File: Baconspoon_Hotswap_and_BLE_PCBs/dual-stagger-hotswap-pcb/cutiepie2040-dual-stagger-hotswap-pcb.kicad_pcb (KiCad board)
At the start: 2 copper layers, 200 x 81 mm, 119 parts, among them J1 SM04B-SRSS-TB(LF)(SN), J2 SWD, SW1 BOOT, SW2 RESET, U1 RP2040, U2 W25Q128JVS, U3 XC6206P332MR, Y1 12MHz

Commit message: upload accurate fabrication files for dual-stagger hotswap PCB
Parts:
- MX49: moved to B.Cu
- SW1: value BOOT -> BOOTSEL
- turned MX49 to 180 degrees
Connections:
- MX41 pad 2: unconnected-(MX41-ROW-Pad2) -> Net-(D7-A)
- MX42 pad 2: unconnected-(MX42-ROW-Pad2) -> Net-(D11-A)
- MX43 pad 2: unconnected-(MX43-ROW-Pad2) -> Net-(D15-A)
- MX44 pad 2: unconnected-(MX44-ROW-Pad2) -> Net-(D18-A)
- MX45 pad 2: unconnected-(MX45-ROW-Pad2) -> Net-(D22-A)
- MX46 pad 2: unconnected-(MX46-ROW-Pad2) -> Net-(D26-A)
- MX47 pad 2: unconnected-(MX47-ROW-Pad2) -> Net-(D29-A)

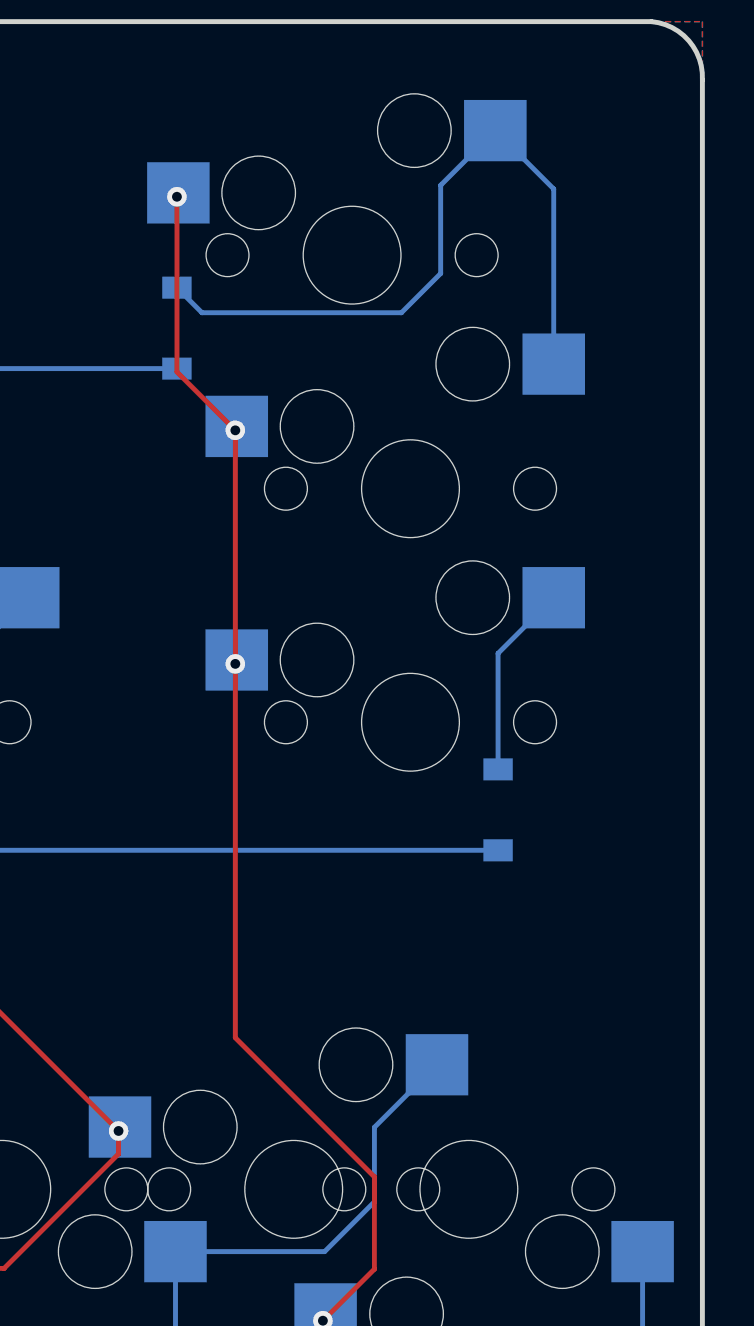
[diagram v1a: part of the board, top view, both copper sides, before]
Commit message: Updated fabrication files for dual-stagger and ortho PCBs and plates. Added stabilizer support for dual-stagger ISO P-key. Updated readme. Updated part mumbers in BOMs and corrected position files. Added KLEs for PCB layouts.
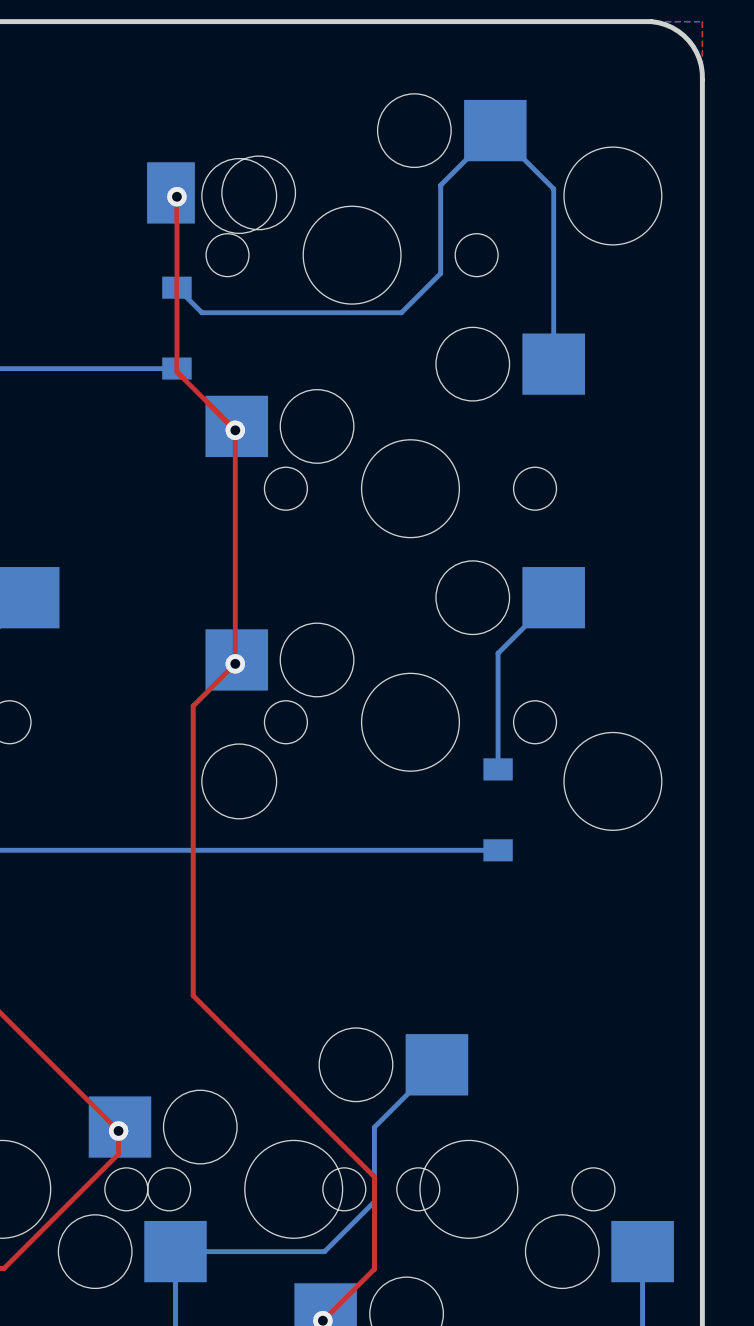
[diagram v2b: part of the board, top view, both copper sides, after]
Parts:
- added H1: ISO Stabilizer Drill, MX_Only:MXOnly-ISO-NoSwitch, F.Cu at (235.7, 54.8)
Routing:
- net col9: track 232.2 -> 233.6 mm
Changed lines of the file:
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@@
   (net 89 "+")
   (net 90 "-")
+  (footprint "MX_Only:MXOnly-ISO-NoSwitch" (layer "F.Cu")
+    (at 235.744344 54.768888)
+    (property "Field2" "")
+    (property "Sheetfile" "MCU-hotswap.kicad_sch")
+    (property "Sheetname" "MCU Component (Hotswap)")
+    (property "ki_description" "Mounting Hole without connection")
+    (property "ki_keywords" "mounting hole")
+    (attr through_hole)
+    (fp_text reference "H1" (at 0 3.175) (layer "Dwgs.User")
+        (effects (font (size 1 1) (thickness 0.15)))
+    )
+    (fp_text value "ISO Stabilizer Drill" (at 0 -7.9375) (layer "Dwgs.User")
+        (effects (font (size 1 1) (thickness 0.15)))
+    )
+    (fp_line (start -16.66875 -19.05) (end -16.66875 0)
+      (stroke (width 0.15) (type solid)) (layer "Dwgs.User"))
+    (fp_line (start -16.66875 -19.05) (end 11.90625 -19.05)
+      (stroke (width 0.15) (type solid)) (layer "Dwgs.User"))
+    (fp_line (start -11.90625 0) (end -16.66875 0)
+      (stroke (width 0.15) (type solid)) (layer "Dwgs.User"))
+    (fp_line (start -11.90625 19.05) (end -11.90625 0)
+      (stroke (width 0.15) (type solid)) (layer "Dwgs.User"))
+    (fp_line (start -11.90625 19.05) (end 11.90625 19.05)
+      (stroke (width 0.15) (type solid)) (layer "Dwgs.User"))
+    (fp_line (start 11.90625 -19.05) (end 11.90625 19.05)
+      (stroke (width 0.15) (type solid)) (layer "Dwgs.User"))
+    (pad "" np_thru_hole circle (at -6.985 -11.938) (size 3.048 3.048) (drill 3.048) (layers "*.Cu" "*.Mask"))
+    (pad "" np_thru_hole circle (at -6.985 11.938) (size 3.048 3.048) (drill 3.048) (layers "*.Cu" "*.Mask"))
+    (pad "" np_thru_hole circle (at 8.255 -11.938) (size 3.9878 3.9878) (drill 3.9878) (layers "*.Cu" "*.Mask"))
+    (pad "" np_thru_hole circle (at 8.255 11.938) (size 3.9878 3.9878) (drill 3.9878) (layers "*.Cu" "*.Mask"))
+  )
   (footprint "MX_Only:MXOnly-1.5U-Hotswap" (layer "B.Cu")
     (at 233.3625 45.24375 180)
@@
     (pad "" np_thru_hole circle (at 3.81 2.54 180) (size 3 3) (drill 3) (layers "*.Cu" "*.Mask"))
     (pad "" np_thru_hole circle (at 5.08 0 228.0996) (size 1.75 1.75) (drill 1.75) (layers "*.Cu" "*.Mask"))
-    (pad "1" smd rect (at 7.085 2.54 180) (size 2.55 2.5) (layers "B.Cu" "B.Paste" "B.Mask")
+    (pad "1" smd rect (at 7.385 2.54 180) (size 1.95 2.5) (layers "B.Cu" "B.Paste" "B.Mask")
       (net 25 "col9") (pinfunction "COL") (pintype "passive"))
     (pad "2" smd rect (at -5.842 5.08 180) (size 2.55 2.5) (layers "B.Cu" "B.Paste" "B.Mask")
@@
   (segment (start 84.90288 78.94975) (end 76.698461 78.94975) (width 0.2) (layer "B.Cu") (net 24))
   (segment (start 93.464141 92.273515) (end 93.964141 92.773515) (width 0.2) (layer "B.Cu") (net 24))
+  (segment (start 226.881344 75.441826) (end 234.2742 82.834682) (width 0.2) (layer "F.Cu") (net 25))
+  (segment (start 226.881344 63.6314) (end 226.881344 75.441826) (width 0.2) (layer "F.Cu") (net 25))
   (segment (start 234.2742 86.599507) (end 232.17207 88.701637) (width 0.2) (layer "F.Cu") (net 25))
   (segment (start 83.769 78.411183) (end 83.34382 77.986003) (width 0.2) (layer "F.Cu") (net 25))
   (segment (start 226.21894 50.006292) (end 228.600192 52.387544) (width 0.2) (layer "F.Cu") (net 25))
+  (segment (start 228.600192 61.912552) (end 226.881344 63.6314) (width 0.2) (layer "F.Cu") (net 25))
   (segment (start 228.600192 61.912552) (end 228.600192 52.387544) (width 0.2) (layer "F.Cu") (net 25))
-  (segment (start 228.600192 77.160674) (end 234.2742 82.834682) (width 0.2) (layer "F.Cu") (net 25))
   (segment (start 92.273515 92.273515) (end 92.273515 90.127829) (width 0.2) (layer "F.Cu") (net 25))
   (segment (start 84.752468 85.69165) (end 83.3771 84.316282) (width 0.2) (layer "F.Cu") (net 25))
@@
   (segment (start 87.837336 85.69165) (end 84.752468 85.69165) (width 0.2) (layer "F.Cu") (net 25))
   (segment (start 92.273515 90.127829) (end 87.837336 85.69165) (width 0.2) (layer "F.Cu") (net 25))
-  (segment (start 228.600192 61.912552) (end 228.600192 77.160674) (width 0.2) (layer "F.Cu") (net 25))
   (segment (start 232.17207 88.701637) (end 232.17207 98.821958) (width 0.2) (layer "F.Cu") (net 25))
   (segment (start 83.769 81.571702) (end 83.769 78.411183) (width 0.2) (layer "F.Cu") (net 25))
